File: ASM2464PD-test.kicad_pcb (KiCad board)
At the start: 4 copper layers, 34.6 x 22 mm, 52 parts, among them J1 USB_C_Receptacle, J2 Bus_M.2_Socket_M, U2 SPI_SOIC-8, U3 SPI_DFN-8

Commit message: silly
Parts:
- added G***: LOGO, LOGO, F.Cu at (72.1, 87.8)
- added G***: LOGO, LOGO, F.Cu at (51.9, 89.0)
- added G***: LOGO, LOGO, F.Cu at (48.1, 73.3)
- added G***: LOGO, LOGO, F.Cu at (49.6, 81.1)
- added G***: LOGO, LOGO, F.Cu at (66.6, 71.8)
- added G***: LOGO, LOGO, F.Cu at (66.9, 86.4)
- added G***: LOGO, LOGO, F.Cu at (76.4, 73.4)
- added G***: LOGO, LOGO, F.Cu at (61.4, 88.2)
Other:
- board text added: "Add cat ears"

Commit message: unsilly
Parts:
- removed G*** (x8): LOGO, LOGO

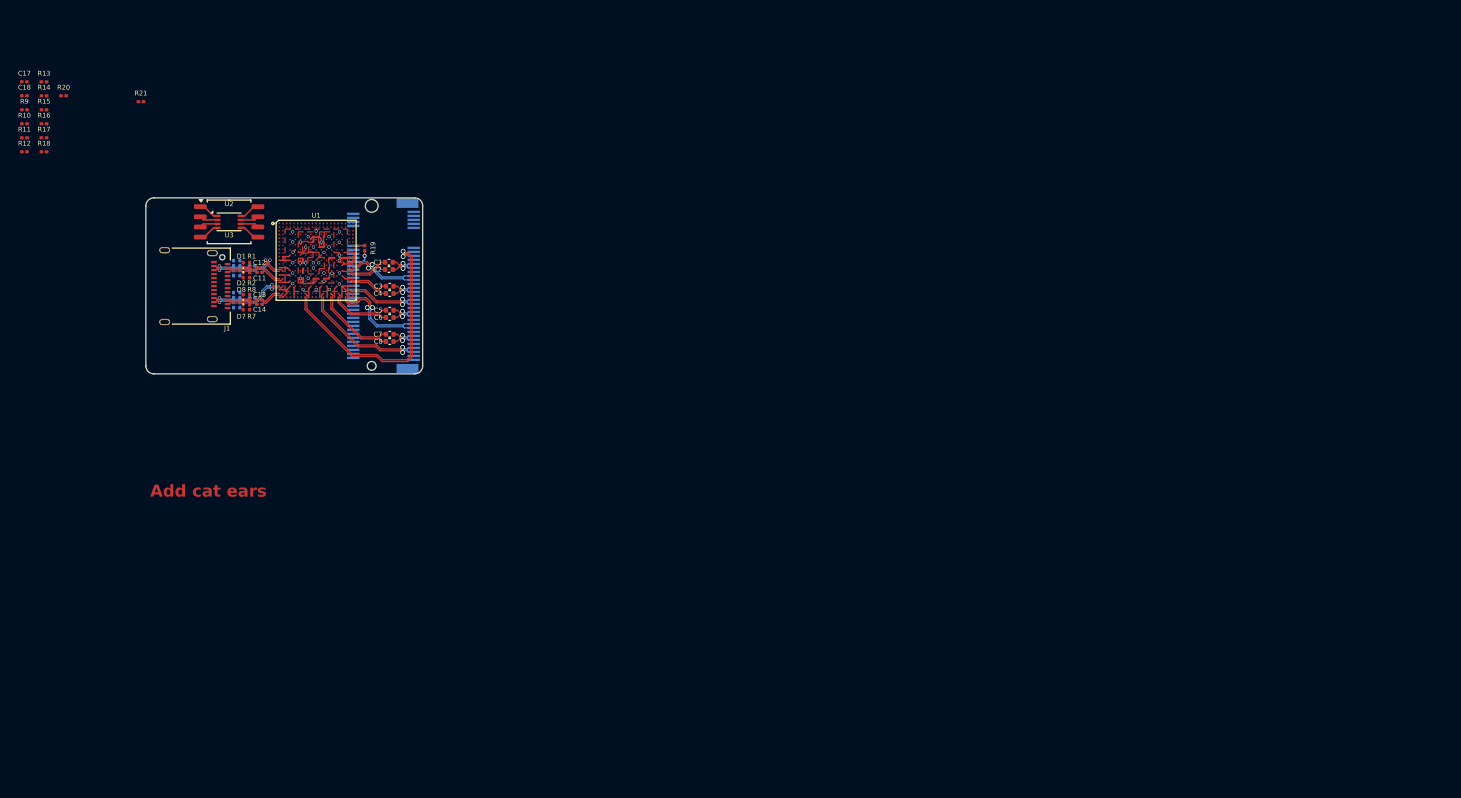
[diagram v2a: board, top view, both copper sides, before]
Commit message: Changing from M.2 adapter to PCIe x4 adapter
I don't actually want an ssd enclosure, I want a PCIe-slot-giver for my laptop
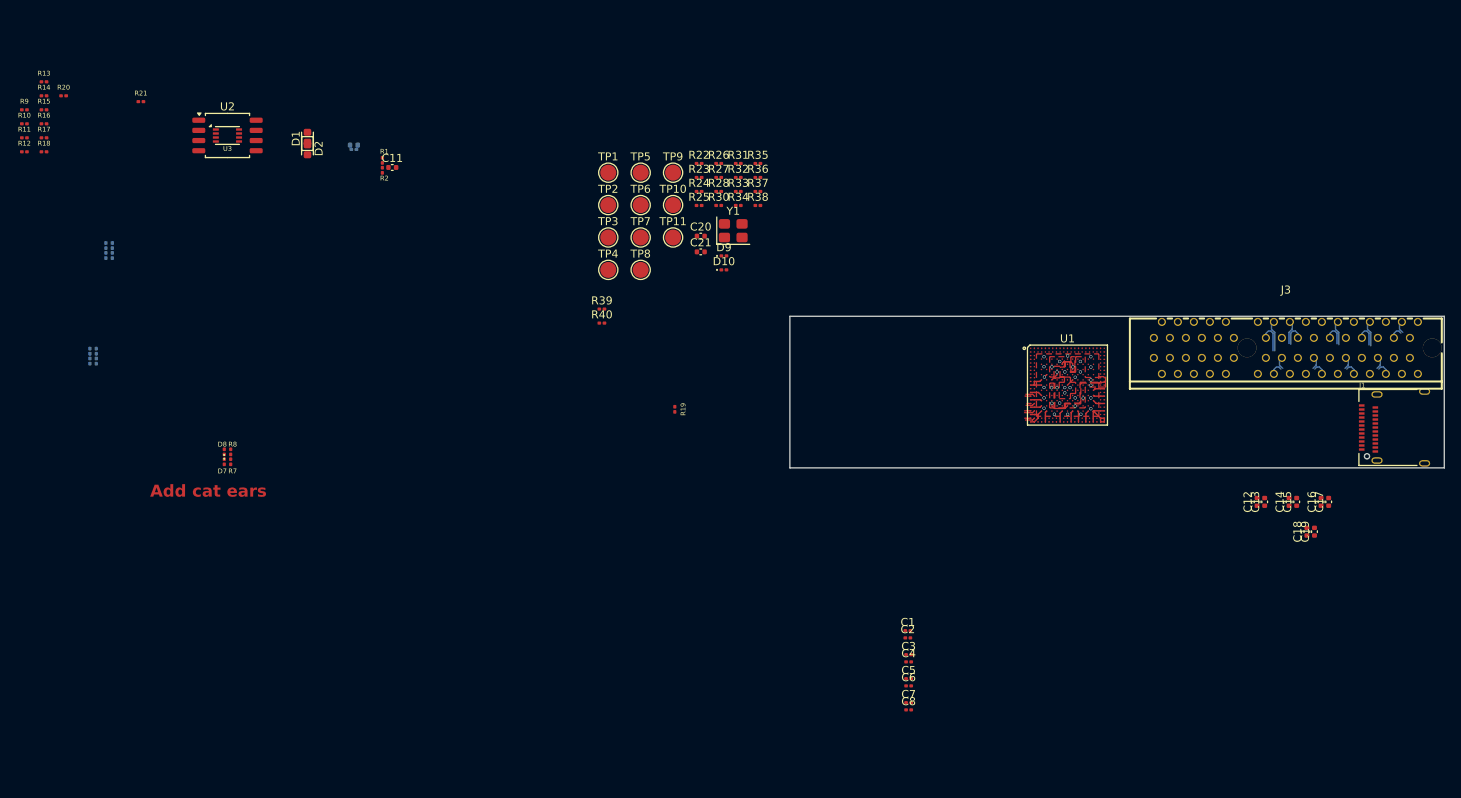
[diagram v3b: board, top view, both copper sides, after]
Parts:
- removed J2: Bus_M.2_Socket_M, A_my_stuff:m-key
- added C19: 0.22u, Capacitor_SMD:C_0402_1005Metric, F.Cu at (191.5, 111.7)
- added C20: 0.1u, Capacitor_SMD:C_0402_1005Metric, F.Cu at (114.8, 74.8)
- added C21: 1u, Capacitor_SMD:C_0402_1005Metric, F.Cu at (114.8, 76.8)
- added D10: ~, Diode_SMD:D_0201_0603Metric, F.Cu at (117.7, 79.0)
- added D9: ~, Diode_SMD:D_0201_0603Metric, F.Cu at (117.7, 77.2)
- added J3: Bus_PCI_Express_x4, A-my-stuff:PCIe_x4_tht_open, F.Cu at (187.9, 88.8)
- added R22: 10k, Resistor_SMD:R_0201_0603Metric, F.Cu at (114.5, 65.7)
- added R23: 10k, Resistor_SMD:R_0201_0603Metric, F.Cu at (114.5, 67.5)
- added R24: 1k, Resistor_SMD:R_0201_0603Metric, F.Cu at (114.5, 69.2)
- added R25: 0Ω, Resistor_SMD:R_0201_0603Metric, F.Cu at (114.5, 71.0)
- added R26: 1k, Resistor_SMD:R_0201_0603Metric, F.Cu at (117.0, 65.7)
- added R27: 4.7k, Resistor_SMD:R_0201_0603Metric, F.Cu at (117.0, 67.5)
- added R28: 4.7k, Resistor_SMD:R_0201_0603Metric, F.Cu at (117.0, 69.2)
- added R30: 0Ω, Resistor_SMD:R_0201_0603Metric, F.Cu at (117.0, 71.0)
- added R31: 0Ω, Resistor_SMD:R_0201_0603Metric, F.Cu at (119.5, 65.7)
- added R32: 12.1k, Resistor_SMD:R_0201_0603Metric, F.Cu at (119.5, 67.5)
- added R33: 100k, Resistor_SMD:R_0201_0603Metric, F.Cu at (119.5, 69.2)
- added R34: 4.7k, Resistor_SMD:R_0201_0603Metric, F.Cu at (119.5, 71.0)
- added R35: 4.7k, Resistor_SMD:R_0201_0603Metric, F.Cu at (121.9, 65.7)
- added R36: 4.7k, Resistor_SMD:R_0201_0603Metric, F.Cu at (121.9, 67.5)
- added R37: 4.7k, Resistor_SMD:R_0201_0603Metric, F.Cu at (121.9, 69.2)
- added R38: 4.7k, Resistor_SMD:R_0201_0603Metric, F.Cu at (121.9, 71.0)
- added R39: 0Ω, Resistor_SMD:R_0201_0603Metric, F.Cu at (102.4, 83.9)
- added R40: 0Ω, Resistor_SMD:R_0201_0603Metric, F.Cu at (102.4, 85.7)
- added TP1: GPIO15, TestPoint:TestPoint_Pad_D2.0mm, F.Cu at (103.2, 66.8)
- added TP10: I2C_DATA, TestPoint:TestPoint_Pad_D2.0mm, F.Cu at (111.3, 70.9)
- added TP11: I2C_CLK, TestPoint:TestPoint_Pad_D2.0mm, F.Cu at (111.3, 75.0)
- added TP2: GPIO16, TestPoint:TestPoint_Pad_D2.0mm, F.Cu at (103.2, 70.9)
- added TP3: GPIO17, TestPoint:TestPoint_Pad_D2.0mm, F.Cu at (103.2, 75.0)
- added TP4: GPIO18, TestPoint:TestPoint_Pad_D2.0mm, F.Cu at (103.2, 79.0)
- added TP5: GPIO25, TestPoint:TestPoint_Pad_D2.0mm, F.Cu at (107.2, 66.8)
- added TP6: GPIO26, TestPoint:TestPoint_Pad_D2.0mm, F.Cu at (107.2, 70.9)
- added TP7: UART_RX, TestPoint:TestPoint_Pad_D2.0mm, F.Cu at (107.2, 75.0)
- added TP8: GPIO1, TestPoint:TestPoint_Pad_D2.0mm, F.Cu at (107.2, 79.0)
- added TP9: GPIO2, TestPoint:TestPoint_Pad_D2.0mm, F.Cu at (111.3, 66.8)
- added Y1: 25MHz, Crystal:Crystal_SMD_3225-4Pin_3.2x2.5mm, F.Cu at (118.8, 74.1)
- C1: value 0.22u -> 10p; footprint Capacitor_SMD:C_0402_1005Metric -> Capacitor_SMD:C_0201_0603Metric
- C10: value 0.33u -> 1u; footprint Capacitor_SMD:C_0201_0603Metric -> Capacitor_SMD:C_0402_1005Metric
- C11: value 0.33u -> 220p; footprint Capacitor_SMD:C_0201_0603Metric -> Capacitor_SMD:C_0402_1005Metric
- C12, C13, C14: value 0.33u -> 0.22u; footprint Capacitor_SMD:C_0201_0603Metric -> Capacitor_SMD:C_0402_1005Metric
- C15, C16: value 0.33u -> 0.22u; footprint Capacitor_SMD:C_0201_0603Metric -> Capacitor_SMD:C_0402_1005Metric; moved to F.Cu
- C17: value 1u -> 0.22u; footprint Capacitor_SMD:C_0201_0603Metric -> Capacitor_SMD:C_0402_1005Metric
- C18: value 0.1u -> 0.22u; footprint Capacitor_SMD:C_0201_0603Metric -> Capacitor_SMD:C_0402_1005Metric
- C2, C3, C4, C5, C6, C7, C8: value 0.22u -> 0.33u; footprint Capacitor_SMD:C_0402_1005Metric -> Capacitor_SMD:C_0201_0603Metric
- D1: value ~ -> LED1; footprint Diode_SMD:D_0201_0603Metric -> LED_SMD:LED_0603_1608Metric
- D2: value ~ -> LED3; footprint Diode_SMD:D_0201_0603Metric -> LED_SMD:LED_0603_1608Metric
- R1, R2: value 220k -> 1k
- R10, R21: value 0Ω -> 10k
- R11, R12, R13, R14: value 0Ω -> 220k
- R15, R17, R18: value 4.7k -> 220k
- R16: value 10k -> 220k
- R3, R4, R5, R6, R7, R8: value 220k -> 0Ω
- R9: value 0Ω -> 4.7k
- U1: footprint A_my_stuff:ASM2464PD -> A-my-stuff:ASM2464PD
- U2: footprint Package_SO:SOIC-8_5.23x5.23mm_P1.27mm -> Package_SO:SOIC-8_5.3x5.3mm_P1.27mm
- moved C17 171.3 mm to (193.2, 108.0), turned to 90 degrees
- moved C18 169.3 mm to (190.5, 111.7), turned to 90 degrees
- moved J1 152.8 mm to (202.4, 98.7), turned to 90 degrees
- moved C16 135.9 mm to (192.3, 108.0), turned to 90 degrees
- moved C15 133.0 mm to (189.2, 108.0), turned to 90 degrees
- moved C14 131.0 mm to (188.3, 108.0), turned to 90 degrees
- moved C13 128.2 mm to (185.2, 108.0), turned to 90 degrees
- moved C12 128.1 mm to (184.3, 108.0), turned to 90 degrees
- moved U1 95.2 mm to (160.6, 93.4)
- moved C1 79.5 mm to (140.6, 124.1)
- moved C2 79.5 mm to (140.6, 125.0)
- moved C3 79.5 mm to (140.7, 127.1)
- moved C4 79.5 mm to (140.7, 128.0)
- moved C5 79.5 mm to (140.7, 130.1)
- moved C6 79.5 mm to (140.7, 131.0)
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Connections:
- C1 pad 1: PCIe_TX0+ -> XO
- C1 pad 2: /PCIe_TX0_C+ -> XI
- C10 pad 1: /URX0_C+ -> VBUS
- C10 pad 2: URX0+ -> GND
- C11 pad 1: /UTX0_C- -> PERST#
- C11 pad 2: UTX0- -> GND
- C12 pad 1: /UTX0_C+ -> PCIe_TX0+
- C12 pad 2: UTX0+ -> /Main/PCIe_TX0_C+
- C13 pad 1: /URX1_C- -> PCIe_TX0-
- C13 pad 2: URX1- -> /Main/PCIe_TX0_C-
- C14 pad 1: /URX1_C+ -> PCIe_TX1+
- C14 pad 2: URX1+ -> /Main/PCIe_TX1_C+
- C15 pad 1: /UTX1_C- -> PCIe_TX1-
- C15 pad 2: UTX1- -> /Main/PCIe_TX1_C-
- C16 pad 1: /UTX1_C+ -> PCIe_TX2+
- C16 pad 2: UTX1+ -> /Main/PCIe_TX2_C+
- C17 pad 1: VBUS -> PCIe_TX2-
- C17 pad 2: GND -> /Main/PCIe_TX2_C-
- C18 pad 1: +3.3V -> PCIe_TX3+
- C18 pad 2: GND -> /Main/PCIe_TX3_C+
- C2 pad 1: PCIe_TX0- -> /Main/URX0_C-
- C2 pad 2: /PCIe_TX0_C- -> URX0-
- C3 pad 1: PCIe_TX1+ -> /Main/URX0_C+
- C3 pad 2: /PCIe_TX1_C+ -> URX0+
- C4 pad 1: PCIe_TX1- -> /Main/UTX0_C-
- C4 pad 2: /PCIe_TX1_C- -> UTX0-
- C5 pad 1: PCIe_TX2+ -> /Main/UTX0_C+
- C5 pad 2: /PCIe_TX2_C+ -> UTX0+
- C6 pad 1: PCIe_TX2- -> /Main/URX1_C-
- C6 pad 2: /PCIe_TX2_C- -> URX1-
- C7 pad 1: PCIe_TX3+ -> /Main/URX1_C+
- C7 pad 2: /PCIe_TX3_C+ -> URX1+
- C8 pad 1: PCIe_TX3- -> /Main/UTX1_C-
- C8 pad 2: /PCIe_TX3_C- -> UTX1-
- C9 pad 1: /URX0_C- -> /Main/UTX1_C+
- C9 pad 2: URX0- -> UTX1+
- D1 pad 1: /UTX0_C+ -> Net-(D1-K)
- D1 pad 2: GND -> +3.3V
- D2 pad 1: /UTX0_C- -> Net-(D2-K)
- D2 pad 2: GND -> +3.3V
- D3 pad 1: /URX0_C+ -> /Main/UTX0_C+
- D4 pad 1: /URX0_C- -> /Main/UTX0_C-
- D5 pad 1: /UTX1_C+ -> /Main/URX0_C+
- D6 pad 1: /UTX1_C- -> /Main/URX0_C-
- D7 pad 1: /URX1_C+ -> /Main/UTX1_C+
- D8 pad 1: /URX1_C- -> /Main/UTX1_C-
- J1 pad A10: /URX1_C- -> /Main/URX1_C-
- J1 pad A11: /URX1_C+ -> /Main/URX1_C+
- J1 pad A2: /UTX0_C+ -> /Main/UTX0_C+
- J1 pad A3: /UTX0_C- -> /Main/UTX0_C-
- J1 pad A5: /CC1_C -> /Main/CC1_C
- J1 pad A6: /USB2_C_D+ -> /Main/USB2_C_D+
- J1 pad A7: /USB2_C_D- -> /Main/USB2_C_D-
- J1 pad A8: /SBU1_C -> /Main/SBU1_C
- J1 pad B10: /URX0_C- -> /Main/URX0_C-
- J1 pad B11: /URX0_C+ -> /Main/URX0_C+
- J1 pad B2: /UTX1_C+ -> /Main/UTX1_C+
- J1 pad B3: /UTX1_C- -> /Main/UTX1_C-
- J1 pad B5: /CC2_C -> /Main/CC2_C
- J1 pad B6: /USB2_C_D+ -> /Main/USB2_C_D+
- J1 pad B7: /USB2_C_D- -> /Main/USB2_C_D-
- J1 pad B8: /SBU2_C -> /Main/SBU2_C
- R1 pad 1: /UTX0_C+ -> GPIO0
- R1 pad 2: GND -> Net-(D1-K)
- R10 pad 1: /USB2_C_D+ -> VBUS
- R10 pad 2: USB2_D+ -> GND
- R11 pad 1: /SBU1_C -> /Main/UTX0_C+
- R11 pad 2: SBU1 -> GND
- R12 pad 1: /SBU2_C -> /Main/UTX0_C-
- R12 pad 2: SBU2 -> GND
- R13 pad 1: /CC1_C -> /Main/URX0_C+
- R13 pad 2: CC1 -> GND
- R14 pad 1: /CC2_C -> /Main/URX0_C-
- R14 pad 2: CC2 -> GND
- R15 pad 1: +5V_VBUS -> /Main/UTX1_C+
- R15 pad 2: VBUS -> GND
- R16 pad 1: VBUS -> /Main/UTX1_C-
- R17 pad 1: SPI_HOLD# -> /Main/URX1_C+
- R17 pad 2: +3.3V -> GND
- R18 pad 1: SPI_WP# -> /Main/URX1_C-
- R18 pad 2: +3.3V -> GND
- R19 pad 1: PERST# -> HDD_PC_EN
- R19 pad 2: Net-(J2-~{PERST}) -> HDD_PC_EN1
- R2 pad 1: /UTX0_C- -> GPIO3
- R2 pad 2: GND -> Net-(D2-K)
- R20 pad 1: unconnected-(R20-Pad1) -> HDD_PC_EN
- R20 pad 2: Net-(J2-~{CLKREQ}) -> HDD_PC_EN2
- R21 pad 1: unconnected-(R21-Pad1) -> +3.3V
- R21 pad 2: Net-(J2-~{PEWAKE}) -> GPIO8
- R3 pad 1: /URX0_C+ -> /Main/CC1_C
- R3 pad 2: GND -> CC1
- R4 pad 1: /URX0_C- -> /Main/CC2_C
- R4 pad 2: GND -> CC2
- R5 pad 1: /UTX1_C+ -> /Main/USB2_C_D-
- R5 pad 2: GND -> USB2_D-
- R6 pad 1: /UTX1_C- -> /Main/USB2_C_D+
- R6 pad 2: GND -> USB2_D+
- R7 pad 1: /URX1_C+ -> /Main/SBU1_C
- R7 pad 2: GND -> SBU1
- R8 pad 1: /URX1_C- -> /Main/SBU2_C
- R8 pad 2: GND -> SBU2
- R9 pad 1: /USB2_C_D- -> +5V_VBUS
- R9 pad 2: USB2_D- -> VBUS
- U1 pad A1: unconnected-(U1A-GPIO3-PadA1) -> GPIO3
- U1 pad A13: unconnected-(U1A-GPIO22-PadA13) -> GPIO22
- U1 pad A16: unconnected-(U1A-GPIO25-PadA16) -> GPIO25
- U1 pad A17: unconnected-(U1A-GPIO26-PadA17) -> GPIO26
- U1 pad A19: unconnected-(U1A-GPIO8-PadA19) -> GPIO8
- U1 pad A21: unconnected-(U1B-UART_RX-PadA21) -> UART_RX
- U1 pad A6: unconnected-(U1A-GPIO15-PadA6) -> GPIO15
- U1 pad A7: unconnected-(U1A-GPIO16-PadA7) -> GPIO16
- U1 pad A8: unconnected-(U1A-GPIO17-PadA8) -> GPIO17
- U1 pad A9: unconnected-(U1A-GPIO18-PadA9) -> GPIO18
- U1 pad AA3: unconnected-(U1A-REXT-PadAA3) -> UREXT
- U1 pad AA4: unconnected-(U1A-XI-PadAA4) -> XI
- U1 pad B1: unconnected-(U1A-GPIO2-PadB1) -> GPIO2
- U1 pad B21: unconnected-(U1B-UART_TX-PadB21) -> UART_TX
- U1 pad C1: unconnected-(U1A-GPIO1-PadC1) -> GPIO1
- U1 pad C21: unconnected-(U1B-HDDPC-PadC21) -> HDDPC
- U1 pad D1: unconnected-(U1A-GPIO0-PadD1) -> GPIO0
- U1 pad E1: unconnected-(U1B-I2C_CLK_P-PadE1) -> I2C_CLK
- U1 pad F1: unconnected-(U1B-I2C_DATA_P-PadF1) -> I2C_DATA
- U1 pad H1: unconnected-(U1A-RST#-PadH1) -> RST#
- U1 pad Y4: unconnected-(U1A-XO-PadY4) -> XO
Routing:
- net REFCLK+: track 33.4 -> 3.87 mm, vias 1 -> 0
- net REFCLK-: track 32.8 -> 3.92 mm, vias 1 -> 0
- net PCIe_RX3-: track 16.1 -> 1.60 mm, vias 1 -> 0
- net PCIe_RX3+: track 15.2 -> 1.66 mm, vias 1 -> 0
- net PCIe_TX3+: track 10.2 -> 0.00 mm
- net PCIe_TX3-: track 10.0 -> 0.00 mm
- net PCIe_RX2+: track 12.5 -> 3.16 mm, vias 1 -> 0
- net PCIe_RX2-: track 12.3 -> 3.29 mm, vias 1 -> 0
- net PCIe_TX2+: track 7.60 -> 0.00 mm
- net PCIe_TX2-: track 7.43 -> 0.00 mm
- net PCIe_RX0-: track 9.47 -> 3.05 mm, vias 1 -> 0
- net PCIe_RX0+: track 8.92 -> 3.00 mm, vias 1 -> 0
- net PCIe_RX1-: track 8.96 -> 3.14 mm, vias 1 -> 0
- net PCIe_RX1+: track 8.41 -> 3.01 mm, vias 1 -> 0
- net PCIe_TX1+: track 5.25 -> 0.00 mm
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- removed copper zone on In1.Cu, net GND
- removed copper zone on In2.Cu, net GND
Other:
- board size 34.6 x 22 mm -> 81.8 x 19 mm

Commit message: Added link to datasheets and reference schematics to readme + some other changes I forgot what I did lol
thanks @mothenjoyer69 for hosting them!
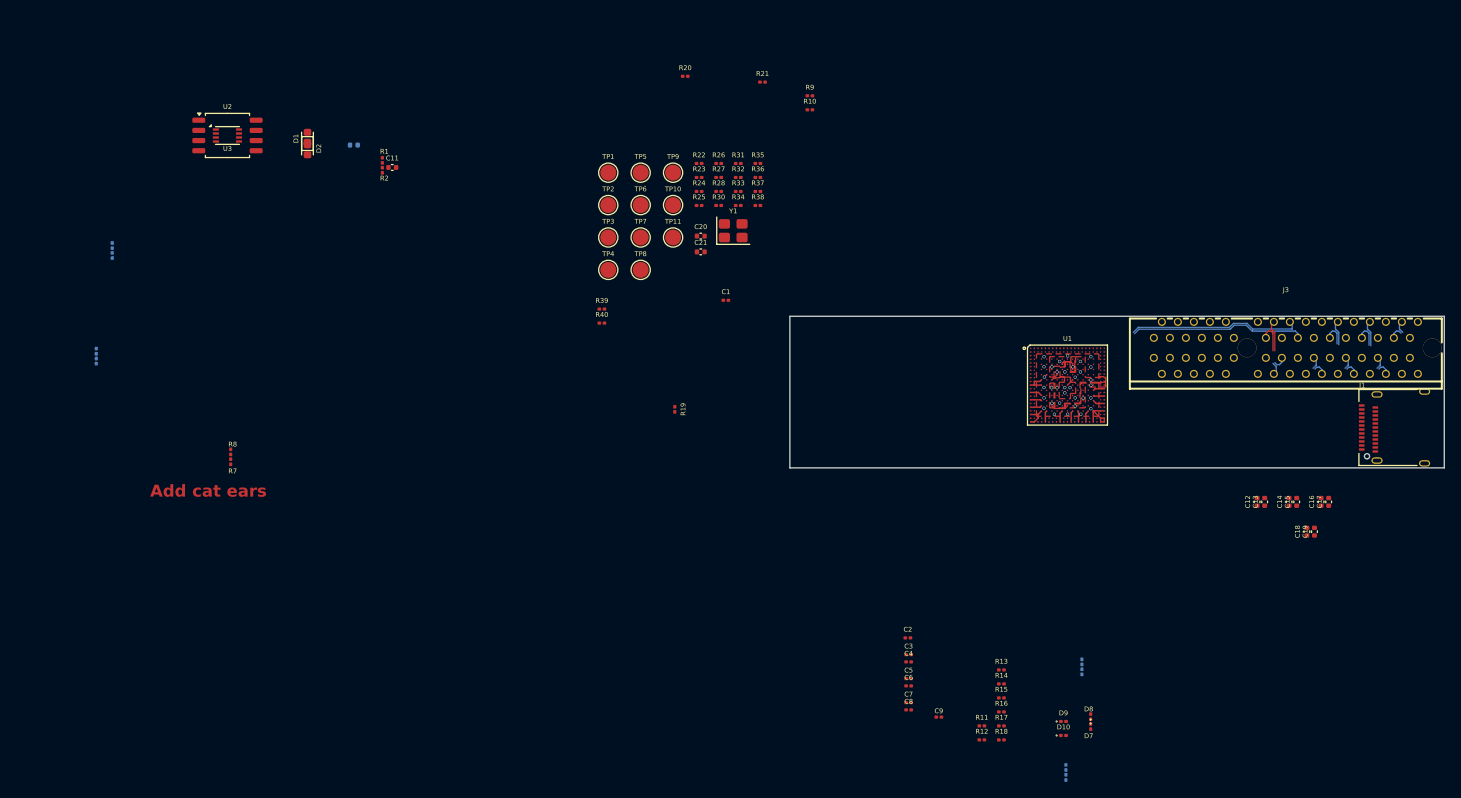
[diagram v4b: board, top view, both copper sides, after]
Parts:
- C9: moved to F.Cu
- moved R11 140.5 mm to (149.9, 136.0)
- moved R12 140.5 mm to (149.9, 137.8)
- moved R13 140.5 mm to (152.3, 129.0)
- moved R14 140.5 mm to (152.3, 130.8)
- moved R15 140.5 mm to (152.3, 132.5)
- moved R16 140.5 mm to (152.3, 134.2)
- moved R17 140.5 mm to (152.3, 136.0)
- moved R18 140.5 mm to (152.3, 137.8)
- moved D3 132.6 mm to (162.4, 128.0)
- moved D4 132.6 mm to (162.4, 129.2)
- moved D5 132.6 mm to (160.4, 142.4)
- moved D6 132.6 mm to (160.4, 141.2)
- moved D7 113.2 mm to (163.5, 136.1)
- moved D8 113.2 mm to (163.5, 134.8)
- moved C9 101.9 mm to (144.5, 134.9)
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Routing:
- net PCIe_RX0-: track 3.05 -> 21.8 mm
- net PCIe_RX0+: track 3.00 -> 21.7 mm
- net UTX1+: track 1.32 -> 0.00 mm
- net URX1+: track 1.20 -> 0.00 mm
- net URX0-: track 1.16 -> 0.00 mm
- net UTX0-: track 1.13 -> 0.00 mm
- net UTX1-: track 0.77 -> 0.00 mm
- net URX1-: track 0.74 -> 0.00 mm
- net URX0+: track 0.70 -> 0.00 mm

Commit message: power notes
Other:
- outline, holes or cut-outs redrawn
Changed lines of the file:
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@@
 	)
 	(gr_line
-		(start 207.7 103.75)
-		(end 125.9 103.75)
+		(start 206.9 103.75)
+		(end 126.7 103.75)
 		(stroke
 			(width 0.1)
@@
 	)
 	(gr_line
-		(start 207.7 84.8)
-		(end 125.9 84.8)
+		(start 206.9 84.8)
+		(end 126.700001 84.8)
+		(stroke
+			(width 0.1)
+			(type default)
+		)
+		(layer "Edge.Cuts")
+	)
+	(gr_arc
+		(start 207.7 102.949999)
+		(mid 207.465686 103.515685)
+		(end 206.900001 103.75)
 		(stroke
 			(width 0.1)
@@
 	)
 	(gr_line
-		(start 207.7 84.8)
-		(end 207.7 103.75)
+		(start 207.7 85.6)
+		(end 207.7 102.949999)
+		(stroke
+			(width 0.1)
+			(type default)
+		)
+		(layer "Edge.Cuts")
+	)
+	(gr_arc
+		(start 125.9 85.6)
+		(mid 126.134315 85.034314)
+		(end 126.700001 84.8)
+		(stroke
+			(width 0.1)
+			(type default)
+		)
+		(layer "Edge.Cuts")
+	)
+	(gr_arc
+		(start 206.9 84.8)
+		(mid 207.465685 85.034315)
+		(end 207.7 85.6)
 		(stroke
 			(width 0.1)
@@
 	)
 	(gr_line
-		(start 125.9 84.8)
-		(end 125.9 103.75)
+		(start 125.9 85.6)
+		(end 125.900002 102.95)
+		(stroke
+			(width 0.1)
+			(type default)
+		)
+		(layer "Edge.Cuts")
+	)
+	(gr_arc
+		(start 126.7 103.75)
+		(mid 126.134315 103.515685)
+		(end 125.9 102.95)
 		(stroke
 			(width 0.1)
@@
 		(type orthogonal)
 		(locked yes)
-		(layer "Edge.Cuts")
+		(layer "User.1")
 		(pts
 			(xy 183.049999 88.750003) (xy 183.05 103.75)
@@
 			(locked yes)
 			(at 217.05 96.250002 90)
-			(layer "Edge.Cuts")
+			(layer "User.1")
 			(effects
 				(font
@@
 		(type orthogonal)
 		(locked yes)
-		(layer "Edge.Cuts")
+		(layer "User.1")
 		(pts
 			(xy 183.049999 88.750003) (xy 125.9 88.750003)
@@
 			(locked yes)
 			(at 154.474999 74.25 0)
-			(layer "Edge.Cuts")
+			(layer "User.1")
 			(effects
 				(font

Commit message: more pin names, more schematic cleanup, added SPI header
baby I don't know when I'm supposed to stop (I should go to bed)
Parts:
- removed TP1: GPIO15, TestPoint:TestPoint_Pad_D2.0mm
- removed TP10: I2C_DATA, TestPoint:TestPoint_Pad_D2.0mm
- removed TP11: I2C_CLK, TestPoint:TestPoint_Pad_D2.0mm
- removed TP2: GPIO16, TestPoint:TestPoint_Pad_D2.0mm
- removed TP3: GPIO17, TestPoint:TestPoint_Pad_D2.0mm
- removed TP4: GPIO18, TestPoint:TestPoint_Pad_D2.0mm
- removed TP5: GPIO25, TestPoint:TestPoint_Pad_D2.0mm
- removed TP6: GPIO26, TestPoint:TestPoint_Pad_D2.0mm
- removed TP7: UART_RX, TestPoint:TestPoint_Pad_D2.0mm
- removed TP8: GPIO1, TestPoint:TestPoint_Pad_D2.0mm
- removed TP9: GPIO2, TestPoint:TestPoint_Pad_D2.0mm
- added D11: ~, LED_SMD:LED_0603_1608Metric, F.Cu at (140.0, 50.3)
- added D12: ~, LED_SMD:LED_0603_1608Metric, F.Cu at (140.0, 52.9)
- added D13: ~, LED_SMD:LED_0603_1608Metric, F.Cu at (140.0, 55.5)
- added D14: ~, LED_SMD:LED_0603_1608Metric, F.Cu at (140.0, 58.0)
- added D15: ~, LED_SMD:LED_0603_1608Metric, F.Cu at (140.0, 60.6)
- added D16: ~, LED_SMD:LED_0603_1608Metric, F.Cu at (140.0, 63.2)
- added J2: SPIheader, Connector_PinHeader_2.54mm:PinHeader_2x04_P2.54mm_Vertical, F.Cu at (144.3, 51.3)
- added R29: 1k, Resistor_SMD:R_0402_1005Metric, F.Cu at (150.4, 49.9)
- added R41: 1k, Resistor_SMD:R_0402_1005Metric, F.Cu at (150.4, 51.6)
- added R42: 1k, Resistor_SMD:R_0402_1005Metric, F.Cu at (150.4, 53.4)
- added R43: 1k, Resistor_SMD:R_0402_1005Metric, F.Cu at (150.4, 55.1)
- C1: footprint Capacitor_SMD:C_0201_0603Metric -> Capacitor_SMD:C_0402_1005Metric
- D1: value LED1 -> ~
- D2: value LED3 -> ~
- R10, R19, R2, R21, R22, R23, R24, R25, R26, R27, R28, R3, R30, R31, R32, R33, R34, R35, R36, R37, R38, R4, R40, R5, R6, R7, R8, R9: footprint Resistor_SMD:R_0201_0603Metric -> Resistor_SMD:R_0402_1005Metric
- R20, R39: value 0Ω -> 1k; footprint Resistor_SMD:R_0201_0603Metric -> Resistor_SMD:R_0402_1005Metric
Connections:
- net 0.95V renamed VDD
- net 1.8V renamed VCCL
- net GPIO0 renamed ActLED1
- net GPIO22 renamed PE_WAKE#
- net GPIO3 renamed ActLED2
- net GPIO8 renamed CLKREQ0#
- net PERST# renamed PERST0#
- C20 pad 1: +3.3V -> +3.3V_LDO
- C21 pad 1: RST# -> GND
- C21 pad 2: GND -> RST#
- D1 pad 2: +3.3V -> +3.3V_LDO
- D2 pad 2: +3.3V -> +3.3V_LDO
- R20 pad 1: HDD_PC_EN -> ActLED3
- R20 pad 2: HDD_PC_EN2 -> Net-(D11-K)
- R21 pad 1: +3.3V -> +3.3V_LDO
- R22 pad 1: +3.3V -> +3.3V_LDO
- R23 pad 1: +3.3V -> +3.3V_LDO
- R27 pad 2: +3.3V -> +3.3V_LDO
- R28 pad 2: +3.3V -> +3.3V_LDO
- R33 pad 2: +3.3V -> +3.3V_LDO
- R34 pad 2: +3.3V -> +3.3V_LDO
- R35 pad 2: +3.3V -> +3.3V_LDO
- R36 pad 1: UART_TX -> GND
- R36 pad 2: GND -> UART_TX
- R37 pad 1: SPI_DO -> GND
- R37 pad 2: GND -> SPI_DO
- R38 pad 1: TEST_EN -> GND
- R38 pad 2: GND -> TEST_EN
- R39 pad 1: +3.3V_SYS -> P1_LED
- R39 pad 2: +3.3V -> Net-(D13-K)
- R40 pad 1: +3.3V_SYS -> +3.3V_LDO
- U1 pad A10: unconnected-(U1A-GPIO19-PadA10) -> GPIO19
- U1 pad A11: unconnected-(U1A-GPIO20-PadA11) -> GPIO20
- U1 pad A12: unconnected-(U1A-GPIO21-PadA12) -> GPIO21
- U1 pad A14: unconnected-(U1A-GPIO23-PadA14) -> CLKREQ2#
- U1 pad A15: unconnected-(U1A-GPIO24-PadA15) -> CLKREQ3#
- U1 pad A16: GPIO25 -> ActLED3
- U1 pad A17: GPIO26 -> ActLED4
- U1 pad A18: unconnected-(U1A-GPIO27-PadA18) -> GPIO27
- U1 pad A20: unconnected-(U1A-GPIO14-PadA20) -> CLKREQ1#
- U1 pad A6: GPIO15 -> P1_LED
- U1 pad A7: GPIO16 -> P2_LED
- U1 pad A8: GPIO17 -> P3_LED
- U1 pad A9: GPIO18 -> P4_LED
- U1 pad D13: +3.3V -> +3.3V_LDO
- U1 pad D6: +3.3V -> +3.3V_LDO
- U1 pad D8: +3.3V -> +3.3V_LDO
- U1 pad D9: +3.3V -> +3.3V_LDO
- U1 pad E13: +3.3V -> +3.3V_LDO
- U1 pad E6: +3.3V -> +3.3V_LDO
- U1 pad E8: +3.3V -> +3.3V_LDO
- U1 pad E9: +3.3V -> +3.3V_LDO
- U1 pad F13: +3.3V -> +3.3V_LDO
- U1 pad F6: +3.3V -> +3.3V_LDO
- U1 pad H6: +3.3V -> +3.3V_LDO
- U2 pad 8: +3.3V -> +3.3V_LDO
- U3 pad 8: +3.3V -> +3.3V_LDO
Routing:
- net +3.3V_LDO: track 0.00 -> 1.69 mm, vias 0 -> 3
- net +3.3V: track 1.69 -> 0.00 mm, vias 3 -> 0
- added copper zone on F.Cu, net +3.3V_LDO
- removed copper zone on F.Cu, net +3.3V
